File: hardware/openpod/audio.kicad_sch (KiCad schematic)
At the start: 29 parts, among them J1 SJ-43515TS-SMT-TR

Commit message: designed clickwheel and see if mpr121 can fit on it
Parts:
- J1: footprint jack:CUI_SJ-43515TS-SMT-TR -> CUI_SJ-43515TS-SMT-TR
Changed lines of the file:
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@@
       (effects (font (size 1.27 1.27)) (justify left))
     )
-    (property "Footprint" "jack:CUI_SJ-43515TS-SMT-TR" (at 76.708 42.418 0)
+    (property "Footprint" "CUI_SJ-43515TS-SMT-TR" (at 76.708 42.418 0)
       (effects (font (size 1.27 1.27)) (justify left bottom) hide)
     )

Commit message: update power and audio
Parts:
- removed Audiocodec1: VS1063, Package_QFP:LQFP-48-1EP_7x7mm_P0.5mm_EP3.6x3.6mm, symbol vs1063:vs1063
- removed R15: 100K, symbol Device:R
- added R1: 100K, symbol Device:R
- added VS1: ~, symbol openpod:vs1063
- renumbered J1 to Jack
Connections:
- net GND: now also VS1.16 (DGND1), VS1.20 (DGND2), VS1.21 (DGND3), VS1.22 (DGND4), VS1.35 (GND), VS1.4 (DGND0); no longer C29.1, C3.1, C30.2, C31.2, C32.2, C33.2, C34.2, C9.1
- net GPIO_PULL: now also VS1.10 (GPIO3/SDATA), VS1.11 (GPIO6/I2S_SCLK), VS1.12 (GPIO7/I2S_SDATA), VS1.25 (GPIO5/I2S_MCLK), VS1.33 (GPIO0), VS1.34 (GPIO1), VS1.36 (GPIO4/I2S_LROUT), VS1.9 (GPIO2/DCLK)
- net at C34.1: now also VS1.44 (RCAP)
- net at Jack.1, R13.2: now also VS1.42 (GBUF)
- net at Jack.2, R14.2: now also VS1.46 (LEFT)
- net at Jack.3, Jack.4, R2.2: now also VS1.39 (RIGHT)
- net VSRESET: now reaches C36.1, Cristal1.1, R18.1
- net VSRESET: now also VS1.18 (XTALI), VS1.3 (XRESET)
- net at C38.1, Cristal1.2, R18.2: now also VS1.17 (XTALO)
- net AVDD renamed +3.3VA
- net +3.3VA: now also VS1.38 (AVDD0), VS1.43 (AVDD1), VS1.45 (AVDD2)
- net CVDD renamed +1V8
- net +1V8: now also VS1.24 (CVDD2), VS1.31 (CVDD3), VS1.5 (CVDD0), VS1.7 (CVDD1)
- net IOVDD renamed +3.3V
- net +3.3V: now also R1.2, VS1.14 (IOVDD1), VS1.19 (IOVDD2), VS1.32 (XTEST), VS1.6 (IOVDD0)
- new net: R1.1, VS1.26 (RX)
- new net GNDA: C29.1, C3.1, C30.2, C31.2, C32.2, C33.2, C34.2, C9.1, VS1.37 (AGND0), VS1.40 (AGND1), VS1.41 (AGND2), VS1.47 (AGND3)
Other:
- moved on the sheet: C30, C31, C32, C33, C34, C35, C36, C37, C38, C39, C40, C41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

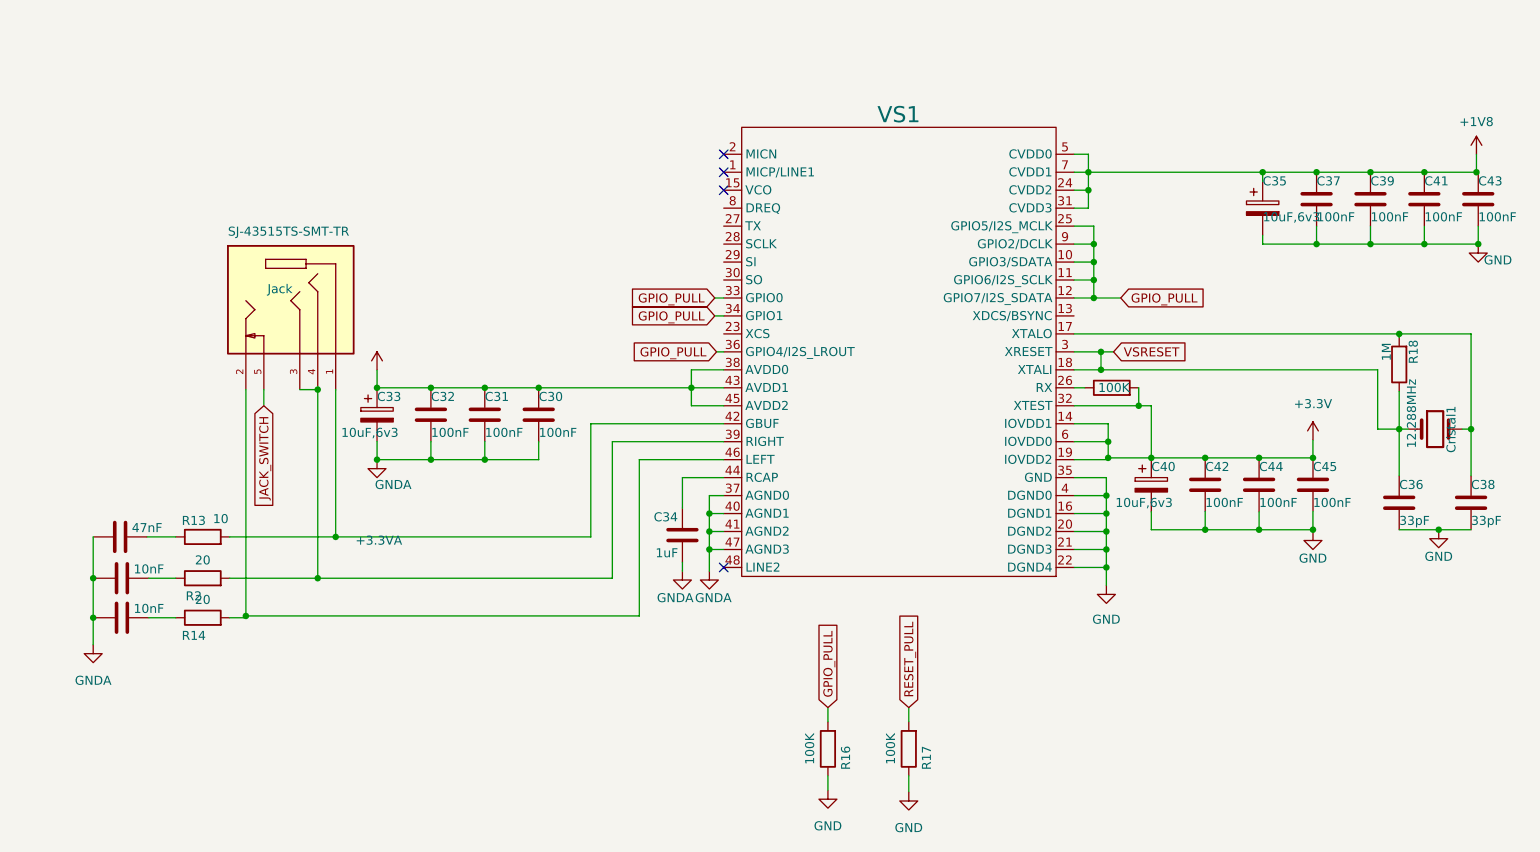
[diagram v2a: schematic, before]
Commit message: added UART converter
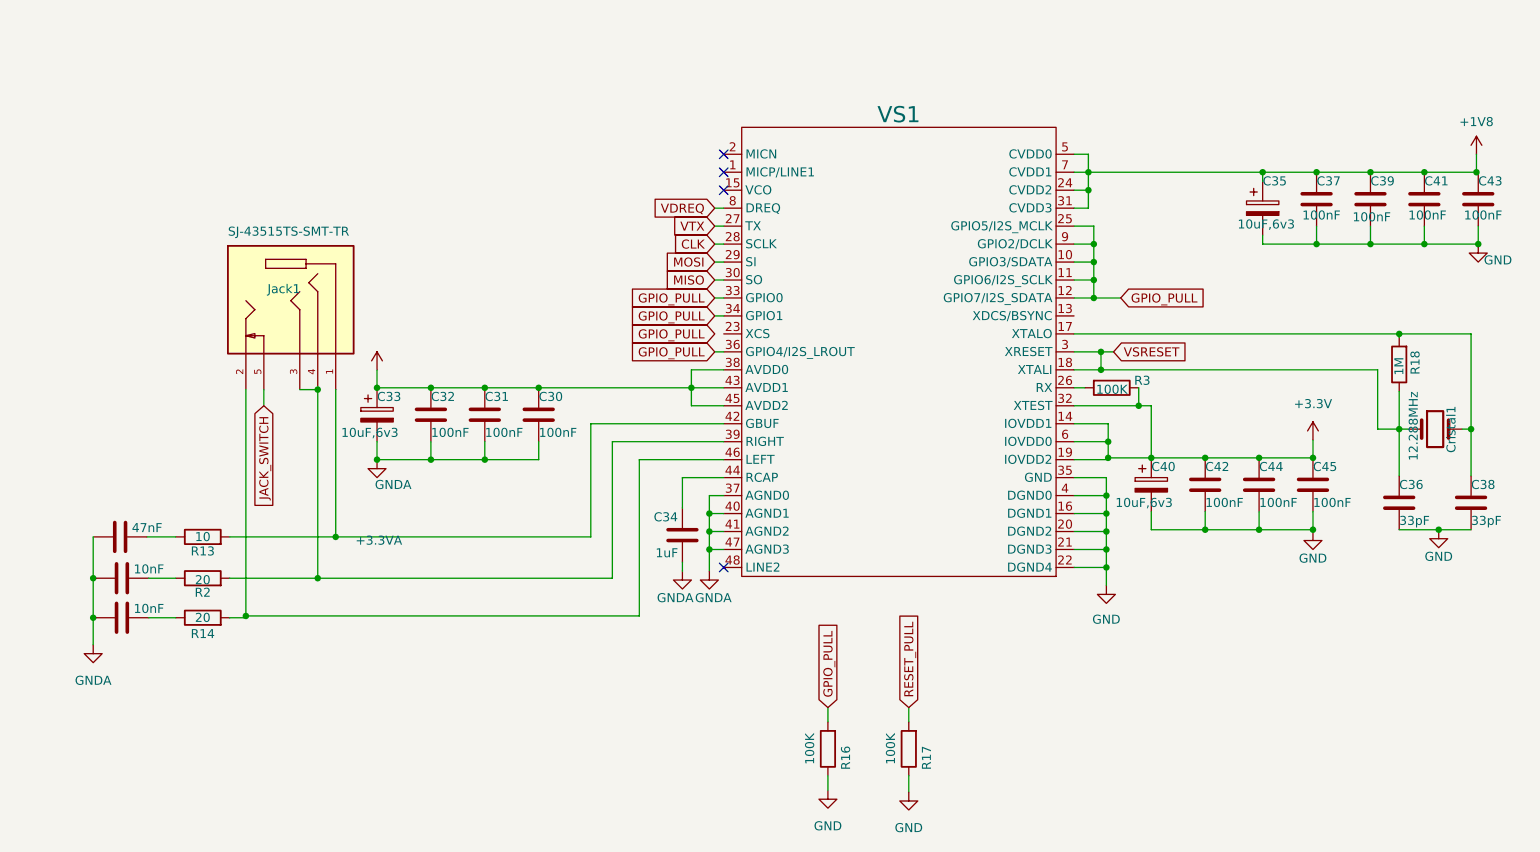
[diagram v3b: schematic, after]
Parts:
- removed R1: 100K, symbol Device:R
- added R3: 100K, symbol Device:R
- renumbered Jack to Jack1
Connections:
- net +3.3V: now also R3.1
- net at VS1.26 (RX): now also R3.2
- net VTX: now reaches VS1.27 (TX)
- net CLK: now reaches VS1.28 (SCLK)
- net MOSI: now reaches VS1.29 (SI)
- net MISO: now reaches VS1.30 (SO)
- net VDREQ: now reaches VS1.8 (DREQ)

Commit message: added bluetooth
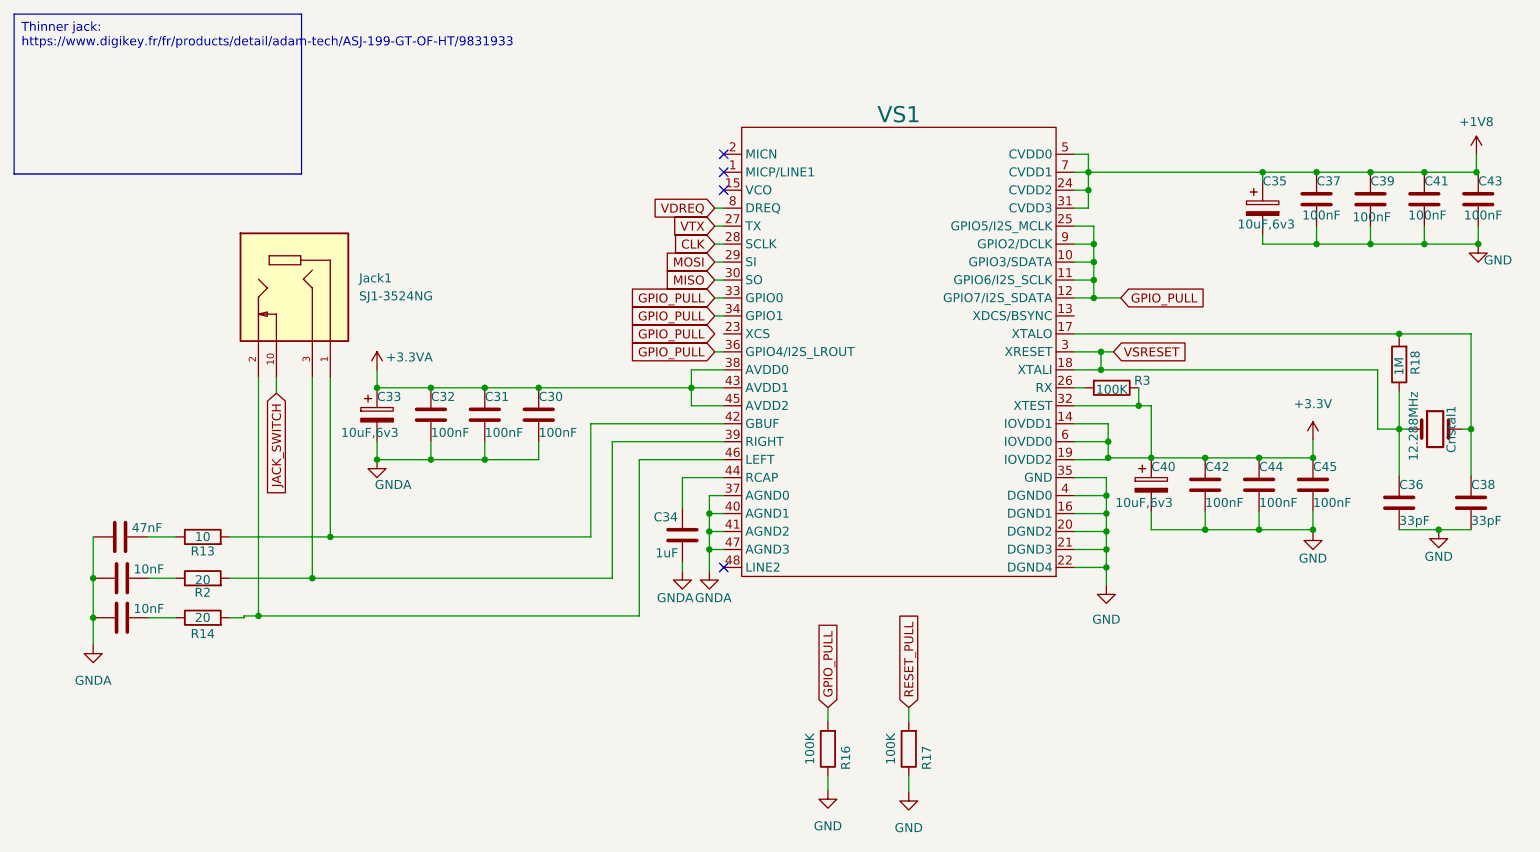
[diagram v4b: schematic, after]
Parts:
- removed Jack1: SJ-43515TS-SMT-TR, CUI_SJ-43515TS-SMT-TR, symbol jack:SJ-43515TS-SMT-TR
- added Jack1: SJ1-3524NG, openpod:CUI_SJ1-3524NG, symbol openpod:SJ1-3524NG
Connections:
- net JACK_SWITCH: now also Jack1.10
- net at R13.2, VS1.42 (GBUF): now also Jack1.1
- net at R14.2, VS1.46 (LEFT): now also Jack1.2
- net at R2.2, VS1.39 (RIGHT): now also Jack1.3
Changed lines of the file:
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@@
   (junction (at 241.808 53.34) (diameter 0) (color 0 0 0 0)
   )
+  (junction (at 69.596 116.078) (diameter 0) (color 0 0 0 0)
+  )
   (junction (at 187.706 71.12) (diameter 0) (color 0 0 0 0)
   )
@@
   (junction (at 189.484 106.68) (diameter 0) (color 0 0 0 0)
   )
-  (junction (at 80.518 104.902) (diameter 0) (color 0 0 0 0)
-  )
-  (junction (at 77.978 110.744) (diameter 0) (color 0 0 0 0)
-  )
   (junction (at 203.454 103.886) (diameter 0) (color 0 0 0 0)
   )
@@
   (junction (at 234.442 53.34) (diameter 0) (color 0 0 0 0)
   )
+  (junction (at 77.216 110.744) (diameter 0) (color 0 0 0 0)
+  )
   (junction (at 46.228 110.744) (diameter 0) (color 0 0 0 0)
   )
-  (junction (at 67.818 116.078) (diameter 0) (color 0 0 0 0)
-  )
   (junction (at 101.6 83.82) (diameter 0) (color 0 0 0 0)
   )
@@
   (junction (at 241.046 89.662) (diameter 0) (color 0 0 0 0)
   )
-  (junction (at 77.978 84.074) (diameter 0) (color 0 0 0 0)
-  )
   (junction (at 242.062 63.5) (diameter 0) (color 0 0 0 0)
   )
@@
   )
   (junction (at 187.706 63.5) (diameter 0) (color 0 0 0 0)
+  )
+  (junction (at 79.756 104.902) (diameter 0) (color 0 0 0 0)
   )
   (junction (at 189.484 104.14) (diameter 0) (color 0 0 0 0)
@@
     (stroke (width 0) (type default))
   )
-  (wire (pts (xy 67.564 116.078) (xy 67.818 116.078))
-    (stroke (width 0) (type default))
-  )
   (wire (pts (xy 161.544 129.032) (xy 161.544 131.064))
     (stroke (width 0) (type default))
   )
-  (wire (pts (xy 80.518 84.074) (xy 80.518 104.902))
+  (wire (pts (xy 79.756 82.296) (xy 79.756 104.902))
     (stroke (width 0) (type default))
   )
@@
     (stroke (width 0) (type default))
   )
-  (wire (pts (xy 75.438 84.074) (xy 77.978 84.074))
-    (stroke (width 0) (type default))
-  )
   (wire (pts (xy 195.834 103.886) (xy 195.834 101.346))
     (stroke (width 0) (type default))
   )
-  (wire (pts (xy 70.358 86.36) (xy 70.358 84.074))
+  (wire (pts (xy 72.136 84.582) (xy 72.136 82.296))
     (stroke (width 0) (type default))
   )
@@
     (stroke (width 0) (type default))
   )
-  (wire (pts (xy 65.532 104.902) (xy 80.518 104.902))
+  (wire (pts (xy 65.532 104.902) (xy 79.756 104.902))
     (stroke (width 0) (type default))
   )
@@
     (stroke (width 0) (type default))
   )
+  (wire (pts (xy 69.596 116.078) (xy 123.444 116.078))
+    (stroke (width 0) (type default))
+  )
   (wire (pts (xy 133.35 101.6) (xy 133.35 104.14))
     (stroke (width 0) (type default))
@@
     (stroke (width 0) (type default))
   )
-  (wire (pts (xy 77.978 110.744) (xy 119.634 110.744))
+  (wire (pts (xy 77.216 110.744) (xy 119.634 110.744))
     (stroke (width 0) (type default))
   )
@@
     (stroke (width 0) (type default))
   )
-  (wire (pts (xy 77.978 84.074) (xy 77.978 110.744))
-    (stroke (width 0) (type default))
-  )
   (wire (pts (xy 130.81 83.82) (xy 130.81 86.36))
     (stroke (width 0) (type default))
@@
     (stroke (width 0) (type default))
   )
-  (wire (pts (xy 116.586 104.902) (xy 80.518 104.902))
+  (wire (pts (xy 79.756 104.902) (xy 116.586 104.902))
     (stroke (width 0) (type default))
   )
@@
     (stroke (width 0) (type default))
   )
+  (wire (pts (xy 77.216 82.296) (xy 77.216 110.744))
+    (stroke (width 0) (type default))
+  )
   (wire (pts (xy 227.838 89.662) (xy 230.886 89.662))
     (stroke (width 0) (type default))
@@
     (stroke (width 0) (type default))
   )
-  (wire (pts (xy 67.818 116.078) (xy 123.444 116.078))
+  (wire (pts (xy 67.564 116.078) (xy 69.596 116.078))
     (stroke (width 0) (type default))
   )
@@
     (stroke (width 0) (type default))
   )
-  (wire (pts (xy 67.818 84.074) (xy 67.818 116.078))
+  (wire (pts (xy 69.596 82.296) (xy 69.596 116.078))
     (stroke (width 0) (type default))
   )
@@
     (stroke (width 0) (type default))
   )
-  (wire (pts (xy 65.532 110.744) (xy 77.978 110.744))
+  (wire (pts (xy 65.532 110.744) (xy 77.216 110.744))
     (stroke (width 0) (type default))
   )
   (wire (pts (xy 230.886 76.2) (xy 230.886 76.708))
     (stroke (width 0) (type default))
+  )
+  (text_box "Thinner jack: https://www.digikey.fr/fr/products/detail/adam-tech/ASJ-199-GT-OF-HT/9831933"
+    (at 35.052 30.988 0) (size 40.64 22.606)
+    (stroke (width 0) (type default))
+    (fill (type none))
+    (effects (font (size 1.27 1.27)) (justify left top))
   )
   (global_label "CLK" (shape input) (at 134.112 63.5 180) (fields_autoplaced)
@@
     )
   )
-  (global_label "JACK_SWITCH" (shape input) (at 70.358 86.36 270) (fields_autoplaced)
+  (global_label "JACK_SWITCH" (shape input) (at 72.136 84.582 270) (fields_autoplaced)
     (effects (font (size 1.27 1.27)) (justify right))
-    (property "Intersheetrefs" "${INTERSHEET_REFS}" (at 70.358 101.7428 90)
+    (property "Intersheetrefs" "${INTERSHEET_REFS}" (at 72.136 99.9648 90)
       (effects (font (size 1.27 1.27)) (justify right) hide)
     )
@@
     )
   )
-  (symbol (lib_id "jack:SJ-43515TS-SMT-TR") (at 75.438 71.374 270) (unit 1)
-    (in_bom yes) (on_board yes) (dnp no)
-    (property "Reference" "Jack1" (at 70.866 69.85 90)
-      (effects (font (size 1.27 1.27)) (justify left))
-    )
-    (property "Value" "SJ-43515TS-SMT-TR" (at 65.278 61.722 90)
-      (effects (font (size 1.27 1.27)) (justify left))
-    )
-    (property "Footprint" "CUI_SJ-43515TS-SMT-TR" (at 75.438 71.374 0)
-      (effects (font (size 1.27 1.27)) (justify left bottom) hide)
-    )
-    (property "Datasheet" "https://www.sameskydevices.com/product/resource/sj-4351x-smt.pdf" (at 75.438 71.374 0)
-      (effects (font (size 1.27 1.27)) (justify left bottom) hide)
-    )
-    (property "PARTREV" "1.05" (at 75.438 71.374 0)
-      (effects (font (size 1.27 1.27)) (justify left bottom) hide)
-    )
-    (property "STANDARD" "Manufacturer Recommendations" (at 75.438 71.374 0)
-      (effects (font (size 1.27 1.27)) (justify left bottom) hide)
-    )
-    (property "MAXIMUM_PACKAGE_HEIGHT" "5.3mm" (at 75.438 71.374 0)
-      (effects (font (size 1.27 1.27)) (justify left bottom) hide)
-    )
-    (property "MANUFACTURER" "CUI Devices" (at 75.438 71.374 0)
-      (effects (font (size 1.27 1.27)) (justify left bottom) hide)
-    )
-    (property "Manufacturer" "Same Sky (Formerly CUI Devices)" (at 75.438 71.374 0)
-      (effects (font (size 1.27 1.27)) hide)
-    )
-    (property "Part number" "SJ-43515TS-SMT-TR" (at 75.438 71.374 0)
-      (effects (font (size 1.27 1.27)) hide)
-    )
-    (property "Supplier" "DigiKey" (at 75.438 71.374 0)
-      (effects (font (size 1.27 1.27)) hide)
-    )
-    (property "Supplier Part number" "CP-43515TSSJTR-ND" (at 75.438 71.374 0)
-      (effects (font (size 1.27 1.27)) hide)
-    )
-    (pin "3")
-    (pin "4")
-    (pin "2")
-    (pin "5")
-    (pin "1")
-    (instances
-      (project "openpod"
-        (path "/0122bb8c-dbef-4db1-a6c6-9be780a38d9f/624e7c04-d7d5-4e26-80cd-388aaab1d060"
-          (reference "Jack1") (unit 1)
-        )
-      )
-    )
-  )
   (symbol (lib_id "Device:C") (at 226.822 57.15 0) (unit 1)
     (in_bom yes) (on_board yes) (dnp no)
@@
       (effects (font (size 1.27 1.27)) hide)
     )
-    (property "Value" "+3.3VA" (at 86.614 105.41 0)
+    (property "Value" "+3.3VA" (at 90.932 79.502 0)
       (effects (font (size 1.27 1.27)))
     )
@@
         )
       )
+    )
+  )
+  (symbol (lib_id "openpod:SJ1-3524NG") (at 74.676 69.596 270) (unit 1)
+    (in_bom yes) (on_board yes) (dnp no) (fields_autoplaced)
+    (property "Reference" "Jack1" (at 83.82 68.326 90)
+      (effects (font (size 1.27 1.27)) (justify left))
+    )
+    (property "Value" "SJ1-3524NG" (at 83.82 70.866 90)
+      (effects (font (size 1.27 1.27)) (justify left))
+    )
+    (property "Footprint" "openpod:CUI_SJ1-3524NG" (at 74.676 69.596 0)
+      (effects (font (size 1.27 1.27)) (justify left bottom) hide)
+    )
+    (property "Datasheet" "https://www.sameskydevices.com/product/resource/sj1-352xng.pdf" (at 74.676 69.596 0)
+      (effects (font (size 1.27 1.27)) (justify left bottom) hide)
+    )
+    (property "Manufacturer" "Same Sky (Formerly CUI Devices)" (at 74.676 69.596 0)
+      (effects (font (size 1.27 1.27)) hide)
+    )
+    (property "Part number" "SJ1-3524NG" (at 74.676 69.596 0)
+      (effects (font (size 1.27 1.27)) hide)
+    )
+    (property "Supplier" "DigiKey" (at 74.676 69.596 0)
+      (effects (font (size 1.27 1.27)) hide)
+    )
+    (property "Supplier Part number" "CP1-3524NG-ND" (at 74.676 69.596 0)
+      (effects (font (size 1.27 1.27)) hide)
+    )
+    (pin "2")
+    (pin "1")
+    (pin "10")
+    (pin "3")
+    (instances
+      (project "openpod"
+        (path "/0122bb8c-dbef-4db1-a6c6-9be780a38d9f/624e7c04-d7d5-4e26-80cd-388aaab1d060"
+          (reference "Jack1") (unit 1)
+        )
+      )
